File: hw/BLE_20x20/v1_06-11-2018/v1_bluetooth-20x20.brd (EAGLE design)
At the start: 27 x 23 mm, 18 parts, among them J2 header, U1 NRF52832

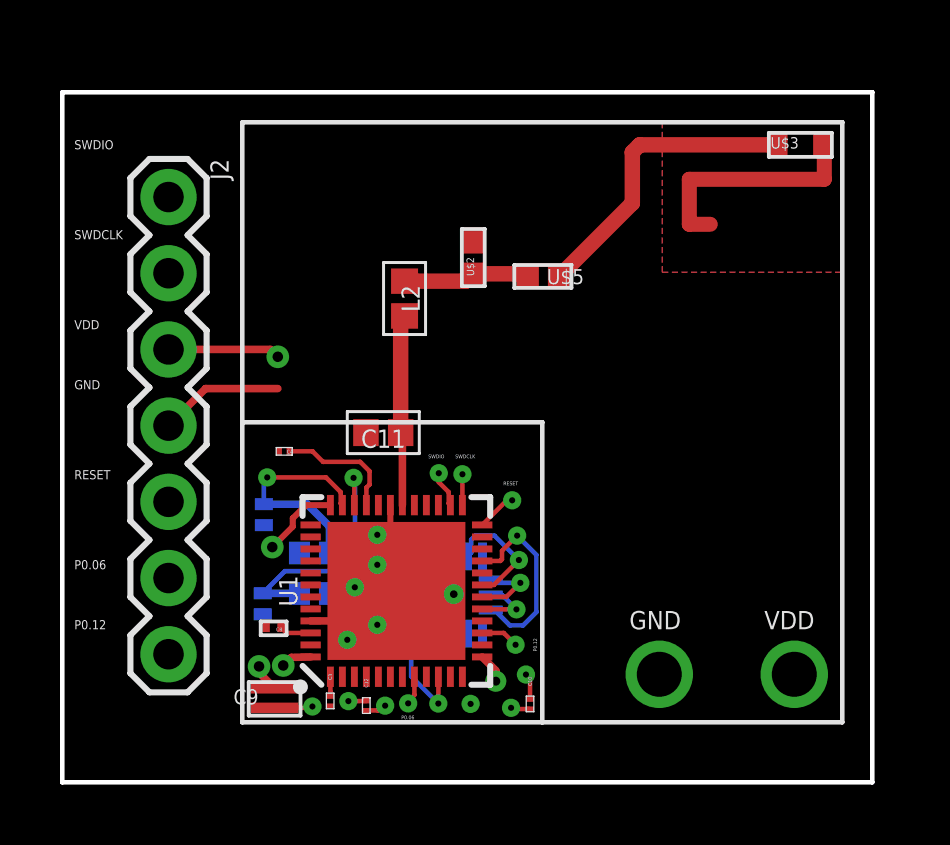
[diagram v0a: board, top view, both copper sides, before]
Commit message: fixed antenna layout and tail
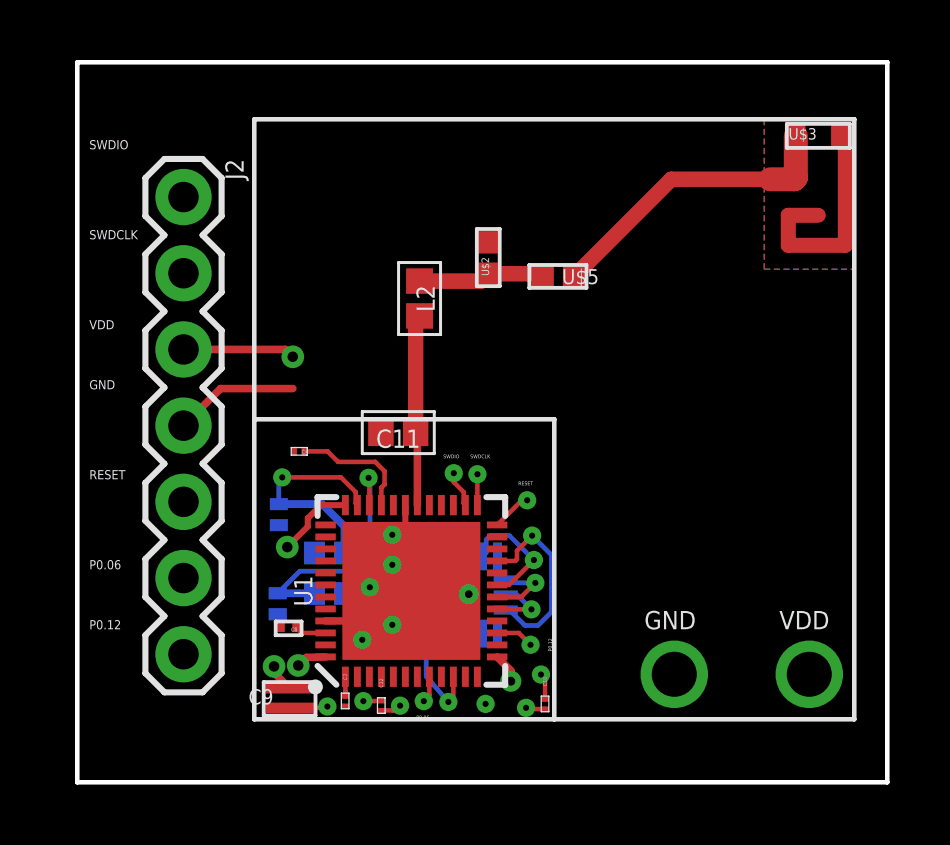
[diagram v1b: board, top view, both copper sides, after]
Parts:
- moved U$3 0.67 mm to (17.8, 19.0)
- moved C12 0.50 mm to (4.23, 0.46)
- moved C9 0.50 mm to (1.28, 0.78)
- moved C1 0.50 mm to (5.93, 6.35)
- moved C10 0.50 mm to (9.69, 0.52)
- moved C11 0.50 mm to (4.80, 9.56)
- moved C3 0.50 mm to (3.03, 0.62)
- moved C4 0.50 mm to (1.51, 8.93)
- moved C6 0.50 mm to (0.82, 6.87)
- moved C7 0.50 mm to (0.78, 3.90)
- moved C8 0.50 mm to (1.09, 3.06)
- moved J2 0.50 mm to (-2.36, 17.4)
- moved L2 0.50 mm to (5.51, 14.0)
- moved U$1 0.50 mm to (7.11, 4.14)
- moved U$2 0.50 mm to (7.80, 16.5)
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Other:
- board size 27 x 23 mm -> 27 x 24 mm
